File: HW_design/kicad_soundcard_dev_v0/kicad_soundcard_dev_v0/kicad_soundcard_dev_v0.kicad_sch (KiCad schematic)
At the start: 1 part

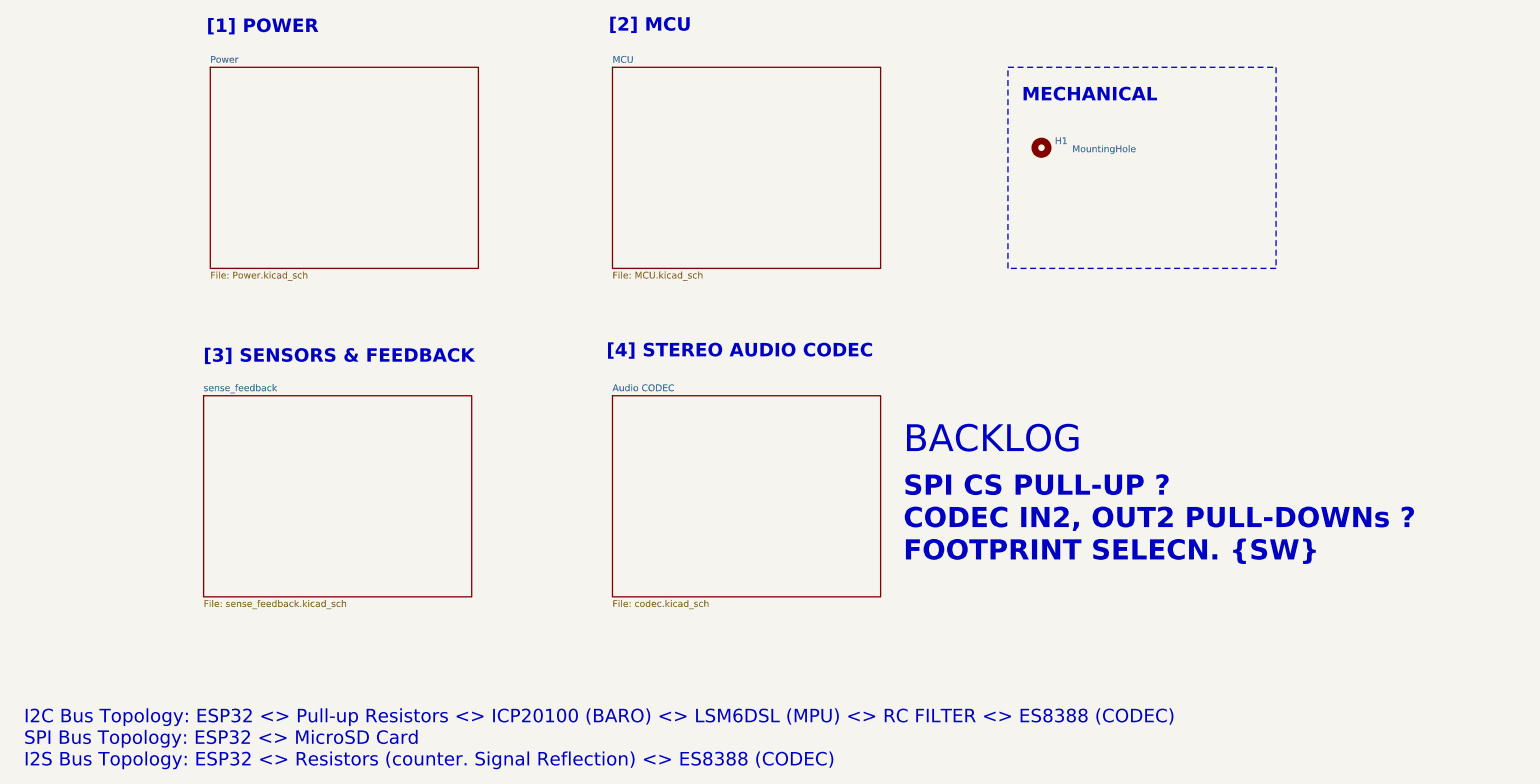
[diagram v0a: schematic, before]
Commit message: Changed Directory structure
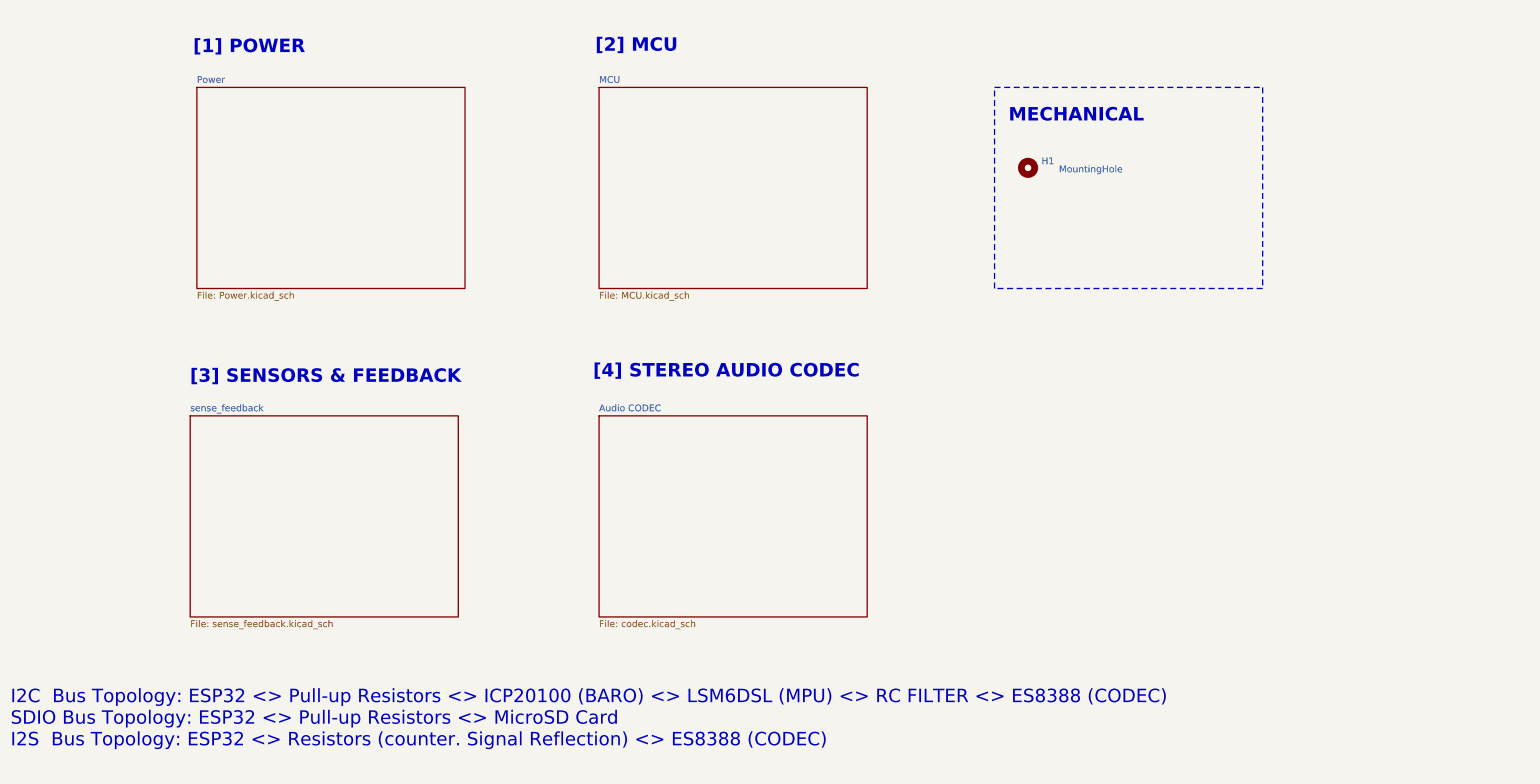
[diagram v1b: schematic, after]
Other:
- note added: "I2C Bus Topology: ESP32 <> Pull-up Resistors <> ICP20100 (BARO) <> LSM6DSL (MPU) <> RC FILTER <> ES8388 (CODEC) SDIO Bus Topology: ESP32 <> Pull-up Resistors <> MicroSD Card I2S Bus Topology: ESP32 <> Resistors (counter. Signal Reflection) <> ES8388 (CODEC)"
- note removed: "BACKLOG"
- note removed: "I2C Bus Topology: ESP32 <> Pull-up Resistors <> ICP20100 (BARO) <> LSM6DSL (MPU) <> RC FILTER <> ES8388 (CODEC) SPI Bus Topology: ESP32 <> MicroSD Card I2S Bus Topology: ESP32 <> Resistors (counter. Signal Reflection) <> ES8388 (CODEC)"
- note removed: "SPI CS PULL-UP ? CODEC IN2, OUT2 PULL-DOWNs ? FOOTPRINT SELECN. {SW}"
- title: BASM SOUNDCARD -> BASM SOUNDCARD DEV V0
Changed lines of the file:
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@@
 	(paper "A4")
 	(title_block
-		(title "BASM SOUNDCARD")
+		(title "BASM SOUNDCARD DEV V0")
+		(date "2025-04-29")
 		(rev "1")
 		(company "BUCHAREST APPLIED STEAM MUSEUM")
-		(comment 1 "Changed 10u Cap. Footprints to 0603")
+		(comment 1 "Replaced MCU w. ESP32 C6 MINI ")
+		(comment 2 "Added SD Card, Aux Insertion Monitoring")
 	)
 	(rectangle
-		(start 203.2 30.48)
-		(end 254 68.58)
+		(start 200.66 34.29)
+		(end 251.46 72.39)
 		(stroke
 			(width 0)
@@
 		)
 	)
+	(text "[4] STEREO AUDIO CODEC\n\n"
+		(exclude_from_sim no)
+		(at 149.86 90.17 0)
+		(effects
+			(font
+				(size 2.54 2.54)
+				(thickness 0.762)
+				(bold yes)
+			)
+		)
+	)
+	(text "[1] POWER"
+		(exclude_from_sim no)
+		(at 59.436 26.67 0)
+		(effects
+			(font
+				(size 2.54 2.54)
+				(thickness 0.762)
+				(bold yes)
+			)
+		)
+	)
+	(text "I2C  Bus Topology: ESP32 <> Pull-up Resistors <> ICP20100 (BARO) <> LSM6DSL (MPU) <> RC FILTER <> ES8388 (CODEC)\nSDIO Bus Topology: ESP32 <> Pull-up Resistors <> MicroSD Card\nI2S  Bus Topology: ESP32 <> Resistors (counter. Signal Reflection) <> ES8388 (CODEC)"
+		(exclude_from_sim no)
+		(at 14.224 153.924 0)
+		(effects
+			(font
+				(size 2.54 2.54)
+				(thickness 0.3175)
+			)
+			(justify left)
+		)
+	)
+	(text "[2] MCU\n"
+		(exclude_from_sim no)
+		(at 132.842 26.416 0)
+		(effects
+			(font
+				(size 2.54 2.54)
+				(thickness 0.762)
+				(bold yes)
+			)
+		)
+	)
+	(text "[3] SENSORS & FEEDBACK\n\n"
+		(exclude_from_sim no)
+		(at 73.914 91.186 0)
+		(effects
+			(font
+				(size 2.54 2.54)
+				(thickness 0.762)
+				(bold yes)
+			)
+		)
+	)
 	(text "MECHANICAL"
 		(exclude_from_sim no)
-		(at 218.694 35.814 0)
-		(effects
-			(font
-				(size 2.54 2.54)
-				(thickness 0.762)
-				(bold yes)
-			)
-		)
-	)
-	(text "SPI CS PULL-UP ?\nCODEC IN2, OUT2 PULL-DOWNs ?\nFOOTPRINT SELECN. {SW}"
-		(exclude_from_sim no)
-		(at 183.388 116.078 0)
-		(effects
-			(font
-				(size 3.81 3.81)
-				(thickness 0.254)
-				(bold yes)
-				(color 255 4 28 1)
-			)
-			(justify left)
-		)
-	)
-	(text "[2] MCU\n"
-		(exclude_from_sim no)
-		(at 135.382 22.606 0)
-		(effects
-			(font
-				(size 2.54 2.54)
-				(thickness 0.762)
-				(bold yes)
-			)
-		)
-	)
-	(text "[4] STEREO AUDIO CODEC\n\n"
-		(exclude_from_sim no)
-		(at 152.4 86.36 0)
-		(effects
-			(font
-				(size 2.54 2.54)
-				(thickness 0.762)
-				(bold yes)
-			)
-		)
-	)
-	(text "I2C Bus Topology: ESP32 <> Pull-up Resistors <> ICP20100 (BARO) <> LSM6DSL (MPU) <> RC FILTER <> ES8388 (CODEC)\nSPI Bus Topology: ESP32 <> MicroSD Card\nI2S Bus Topology: ESP32 <> Resistors (counter. Signal Reflection) <> ES8388 (CODEC)"
-		(exclude_from_sim no)
-		(at 16.764 157.734 0)
-		(effects
-			(font
-				(size 2.54 2.54)
-				(thickness 0.3175)
-			)
-			(justify left)
-		)
-	)
-	(text "[1] POWER"
-		(exclude_from_sim no)
-		(at 61.976 22.86 0)
-		(effects
-			(font
-				(size 2.54 2.54)
-				(thickness 0.762)
-				(bold yes)
-			)
-		)
-	)
-	(text "[3] SENSORS & FEEDBACK\n\n"
-		(exclude_from_sim no)
-		(at 76.454 87.376 0)
-		(effects
-			(font
-				(size 2.54 2.54)
-				(thickness 0.762)
-				(bold yes)
-			)
-		)
-	)
-	(text "BACKLOG"
-		(exclude_from_sim no)
-		(at 183.388 101.092 0)
-		(effects
-			(font
-				(size 5.08 5.08)
-				(thickness 0.635)
-				(color 255 4 28 1)
-			)
-			(justify left)
+		(at 216.154 39.624 0)
+		(effects
+			(font
+				(size 2.54 2.54)
+				(thickness 0.762)
+				(bold yes)
+			)
 		)
 	)
 	(symbol
 		(lib_id "Mechanical:MountingHole")
-		(at 209.55 45.72 0)
+		(at 207.01 49.53 0)
 		(unit 1)
 		(exclude_from_sim yes)
@@
 		(dnp no)
 		(property "Reference" "H1"
-			(at 212.09 44.4499 0)
+			(at 209.55 48.2599 0)
 			(effects
 				(font
@@
 		)
 		(property "Value" "MountingHole"
-			(at 215.392 45.974 0)
+			(at 212.852 49.784 0)
 			(effects
 				(font
@@
 		)
 		(property "Footprint" "MountingHole:MountingHole_3.5mm"
-			(at 209.55 45.72 0)
+			(at 207.01 49.53 0)
 			(effects
 				(font
@@
 		)
 		(property "Datasheet" "~"
-			(at 209.55 45.72 0)
+			(at 207.01 49.53 0)
 			(effects
 				(font
@@
 		)
 		(property "Description" "Mounting Hole without connection"
-			(at 209.55 45.72 0)
+			(at 207.01 49.53 0)
 			(effects
 				(font
@@
 		)
 		(instances
-			(project "basmsoundcard"
-				(path "/a2ae8555-7422-4c55-bf44-8cc769543ba0"
+			(project "kicad_soundcard_dev_v0"
+				(path "/4bede6f6-420d-49b9-8d53-bd69095749c2"
 					(reference "H1")
 					(unit 1)
@@
 	)
 	(sheet
-		(at 128.27 30.48)
+		(at 49.53 34.29)
+		(size 50.8 38.1)
+		(fields_autoplaced yes)
+		(stroke
+			(width 0.1524)
+			(type solid)
+		)
+		(fill
+			(color 0 0 0 0.0000)
+		)
+		(property "Sheetname" "Power"
+			(at 49.53 33.5784 0)
+			(effects
+				(font
+					(size 1.27 1.27)
+				)
+				(justify left bottom)
+			)
+		)
+		(property "Sheetfile" "Power.kicad_sch"
+			(at 49.53 72.9746 0)
+			(effects
+				(font
+					(size 1.27 1.27)
+				)
+				(justify left top)
+			)
+		)
+		(instances
+			(project "kicad_soundcard_dev_v0"
+				(path "/4bede6f6-420d-49b9-8d53-bd69095749c2"
+					(page "1")
+				)
+			)
+		)
+	)
+	(sheet
+		(at 48.26 96.52)
+		(size 50.8 38.1)
+		(fields_autoplaced yes)
+		(stroke
+			(width 0.1524)
+			(type solid)
+		)
+		(fill
+			(color 0 0 0 0.0000)
+		)
+		(property "Sheetname" "sense_feedback"
+			(at 48.26 95.8084 0)
+			(effects
+				(font
+					(size 1.27 1.27)
+				)
+				(justify left bottom)
+			)
+		)
+		(property "Sheetfile" "sense_feedback.kicad_sch"
+			(at 48.26 135.2046 0)
+			(effects
+				(font
+					(size 1.27 1.27)
+				)
+				(justify left top)
+			)
+		)
+		(instances
+			(project "kicad_soundcard_dev_v0"
+				(path "/4bede6f6-420d-49b9-8d53-bd69095749c2"
+					(page "3")
+				)
+			)
+		)
+	)
+	(sheet
+		(at 125.73 34.29)
 		(size 50.8 38.1)
 		(fields_autoplaced yes)
@@
 		)
 		(property "Sheetname" "MCU"
-			(at 128.27 29.7684 0)
+			(at 125.73 33.5784 0)
 			(effects
 				(font
@@
 		)
 		(property "Sheetfile" "MCU.kicad_sch"
-			(at 128.27 69.1646 0)
-			(effects
-				(font
-					(size 1.27 1.27)
-				)
-				(justify left top)
-			)
-		)
-		(instances
-			(project "basmsoundcard"
-				(path "/a2ae8555-7422-4c55-bf44-8cc769543ba0"
+			(at 125.73 72.9746 0)
+			(effects
+				(font
+					(size 1.27 1.27)
+				)
+				(justify left top)
+			)
+		)
+		(instances
+			(project "kicad_soundcard_dev_v0"
+				(path "/4bede6f6-420d-49b9-8d53-bd69095749c2"
 					(page "2")
 				)
@@
 	)
 	(sheet
-		(at 50.8 92.71)
-		(size 50.8 38.1)
-		(fields_autoplaced yes)
-		(stroke
-			(width 0.1524)
-			(type solid)
-		)
-		(fill
-			(color 0 0 0 0.0000)
-		)
-		(property "Sheetname" "sense_feedback"
-			(at 50.8 91.9984 0)
-			(effects
-				(font
-					(size 1.27 1.27)
-				)
-				(justify left bottom)
-			)
-		)
-		(property "Sheetfile" "sense_feedback.kicad_sch"
-			(at 50.8 131.3946 0)
-			(effects
-				(font
-					(size 1.27 1.27)
-				)
-				(justify left top)
-			)
-		)
-		(instances
-			(project "basmsoundcard"
-				(path "/a2ae8555-7422-4c55-bf44-8cc769543ba0"
-					(page "3")
-				)
-			)
-		)
-	)
-	(sheet
-		(at 128.27 92.71)
+		(at 125.73 96.52)
 		(size 50.8 38.1)
 		(fields_autoplaced yes)
@@
 		)
 		(property "Sheetname" "Audio CODEC"
-			(at 128.27 91.9984 0)
+			(at 125.73 95.8084 0)
 			(effects
 				(font
@@
 		)
 		(property "Sheetfile" "codec.kicad_sch"
-			(at 128.27 131.3946 0)
-			(effects
-				(font
-					(size 1.27 1.27)
-				)
-				(justify left top)
-			)
-		)
-		(instances
-			(project "basmsoundcard"
-				(path "/a2ae8555-7422-4c55-bf44-8cc769543ba0"
+			(at 125.73 135.2046 0)
+			(effects
+				(font
+					(size 1.27 1.27)
+				)
+				(justify left top)
+			)
+		)
+		(instances
+			(project "kicad_soundcard_dev_v0"
+				(path "/4bede6f6-420d-49b9-8d53-bd69095749c2"
 					(page "4")
 				)
 			)
-		)
-	)
-	(sheet
-		(at 52.07 30.48)
-		(size 50.8 38.1)
-		(fields_autoplaced yes)
-		(stroke
-			(width 0.1524)
-			(type solid)
-		)
-		(fill
-			(color 0 0 0 0.0000)
-		)
-		(property "Sheetname" "Power"
-			(at 52.07 29.7684 0)
-			(effects
-				(font
-					(size 1.27 1.27)
-				)
-				(justify left bottom)
-			)
-		)
-		(property "Sheetfile" "Power.kicad_sch"
-			(at 52.07 69.1646 0)
-			(effects
-				(font
-					(size 1.27 1.27)
-				)
-				(justify left top)
-			)
-		)
-		(instances
-			(project "basmsoundcard"
-				(path "/a2ae8555-7422-4c55-bf44-8cc769543ba0"
-					(page "1")
-				)
-			)
